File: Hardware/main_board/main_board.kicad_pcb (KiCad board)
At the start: 2 copper layers, 120 x 51.7 mm, 116 parts, among them J1 ALARM, J2 RFID_CONN, J3 GPS_CONN, J4 USB_A, J5 DEBUG, J6 ANTENNA2, J7 Conn_01x08_Male, J8 BATT, J9 RFShield_TwoPieces, Q1 2N3904, SW1 SW_Push, SW2 SW_Push, U1 STM32WL55_UFQFPN48, U2 FT201XQ, U3 SKY13370-374LF, U4 ID-3LA, U5 AP7370-50W5-7, U6 S-1135A33-M5T1U, U7 AP22811BW5-7, U8 AP22811BW5-7, U9 74LVC1G04, Y1 32MHz

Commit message: finished main board
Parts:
- removed ANTENNA1: 1.337m, Connector_Coaxial:SMA_Amphenol_132289_EdgeMount
- removed C11, C35: 10n, Capacitor_SMD:C_0805_2012Metric
- removed C12, C13: 47p, Capacitor_SMD:C_0805_2012Metric
- removed C14: 0.1u, Capacitor_SMD:C_0805_2012Metric
- removed C15, C18: 100n, Capacitor_SMD:C_0805_2012Metric
- removed C16: 4.7u, Capacitor_SMD:C_0805_2012Metric
- removed C36, C46: 1u, Capacitor_SMD:C_0805_2012Metric
- removed C37: DNP, Capacitor_SMD:C_0805_2012Metric
- removed D2, D3: LED, LED_SMD:LED_0805_2012Metric
- removed FB1: FerriteBead, LED_SMD:LED_0805_2012Metric
- removed J4: USB_A, Connector_USB:USB_A_Molex_67643_Horizontal
- removed J9: RFShield_TwoPieces, Capacitor_SMD:C_0805_2012Metric
- removed JP5: SolderJumper_2_Open, Jumper:SolderJumper-2_P1.3mm_Open_TrianglePad1.0x1.5mm
- removed JP8: SolderJumper_3_Open, Jumper:SolderJumper-3_P2.0mm_Open_TrianglePad1.0x1.5mm
- removed Q1: 2N3904, Package_TO_SOT_THT:TO-92_Inline
- removed R10, R11, R5, R6: 1k, Resistor_SMD:R_0805_2012Metric_Pad1.20x1.40mm_HandSolder
- removed R2, R3: 27R, Resistor_SMD:R_0805_2012Metric_Pad1.20x1.40mm_HandSolder
- removed R4: 5k, Resistor_SMD:R_0805_2012Metric_Pad1.20x1.40mm_HandSolder
- removed R7: 500R, Resistor_SMD:R_0805_2012Metric_Pad1.20x1.40mm_HandSolder
- removed R8: 15R, Resistor_SMD:R_0805_2012Metric_Pad1.20x1.40mm_HandSolder
- removed R9: 300R, Resistor_SMD:R_0805_2012Metric_Pad1.20x1.40mm_HandSolder
- removed SW2: SW_Push, Connector_PinSocket_2.54mm:PinSocket_1x02_P2.54mm_Vertical
- removed TP11, TP12: TestPoint, Connector_PinHeader_2.54mm:PinHeader_1x01_P2.54mm_Vertical
- removed U2: FT201XQ, Package_DFN_QFN:QFN-16-1EP_4x4mm_P0.65mm_EP2.1x2.1mm
- removed U4: ID-3LA, new_footprints:ID-3LA
- removed U9: 74LVC1G04, Package_TO_SOT_SMD:SOT-23-5_HandSoldering
- added H1: MountingHole_Pad, MountingHole:MountingHole_2.2mm_M2_DIN965_Pad, F.Cu at (137.7, 147.2)
- added H2: MountingHole_Pad, MountingHole:MountingHole_2.2mm_M2_DIN965_Pad, F.Cu at (221.4, 134.9)
- added H4: MountingHole_Pad, MountingHole:MountingHole_2.2mm_M2_DIN965_Pad, F.Cu at (221.4, 146.3)
- added TP20: TestPoint, TestPoint:TestPoint_Pad_1.0x1.0mm, F.Cu at (174.3, 147.9)
- added TP21: TestPoint, TestPoint:TestPoint_Pad_1.0x1.0mm, F.Cu at (166.4, 147.5)
- added TP8: TestPoint, TestPoint:TestPoint_Pad_1.0x1.0mm, F.Cu at (169.0, 142.2)
- added TP9: TestPoint, TestPoint:TestPoint_Pad_1.0x1.0mm, F.Cu at (174.7, 135.9)
- C10, C17, C22, C23, C24, C25, C26, C27, C28, C29, C3, C30, C31, C32, C33, C34, C38, C39, C4, C40, C41, C42, C43, C5, C6, C7, C8, C9: footprint Capacitor_SMD:C_0805_2012Metric -> Capacitor_SMD:C_0603_1608Metric
- J7: value Conn_01x08_Male -> Conn_01x04_Male; footprint Connector_PinHeader_2.54mm:PinHeader_2x04_P2.54mm_Vertical -> Connector_PinHeader_1.27mm:PinHeader_1x04_P1.27mm_Vertical
- JP1, JP2, JP3, JP4: footprint Jumper:SolderJumper-2_P1.3mm_Open_TrianglePad1.0x1.5mm -> new_footprints:tinyjumper
- TP1, TP13, TP14, TP2, TP3, TP4, TP5, TP6, TP7: footprint Connector_PinHeader_2.54mm:PinHeader_1x01_P2.54mm_Vertical -> TestPoint:TestPoint_Pad_1.0x1.0mm
- moved J7 116.0 mm to (162.6, 148.7), turned to -90 degrees
- moved TP4 35.7 mm to (163.3, 140.6)
- moved TP13 34.0 mm to (142.9, 146.2)
- moved TP2 33.6 mm to (165.6, 142.0)
- moved TP3 33.4 mm to (171.1, 142.2)
- moved SW1 31.4 mm to (132.9, 145.7), turned to 180 degrees
- moved TP7 22.3 mm to (160.9, 140.6)
- moved TP6 19.4 mm to (163.3, 145.1)
- moved J8 17.6 mm to (132.1, 138.9), turned to 180 degrees
- moved J5 16.2 mm to (136.1, 139.1)
- moved TP14 15.1 mm to (133.4, 133.3)
- moved C45 13.7 mm to (149.1, 134.5), turned to 180 degrees
- moved TP5 13.5 mm to (161.1, 145.1)
- moved C44 9.75 mm to (146.3, 148.1), turned to 180 degrees
- moved D4 9.28 mm to (129.2, 144.3), turned to 90 degrees
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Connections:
- J7 pad 1: +3V3_RFID -> I2C1_SCL
- J7 pad 2: Net-(J7-Pad2) -> I2C1_SDA
- J7 pad 3: Net-(J7-Pad3) -> +3V3
- J7 pad 4: Net-(J7-Pad4) -> GND
- TP3 pad 1: Net-(TP3-Pad1) -> DEBUG_JTDI
- U1 pad 12: Net-(TP3-Pad1) -> unconnected-(U1-Pad12)
- U1 pad 31: unconnected-(U1-Pad31) -> RFSW_VC2
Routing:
- net RFSW_VC1: track 7.34 -> 73.1 mm, vias 0 -> 2
- net NRST: track 9.89 -> 72.5 mm, vias 0 -> 1
- net RFID_~{PWR}: track 2.39 -> 50.1 mm, vias 1 -> 2
- net +3V3: track 131.7 -> 177.5 mm, vias 7 -> 4
- net ALARM_ON: track 0.00 -> 45.1 mm, vias 0 -> 1
- net RFSW_VC2: track 12.6 -> 57.4 mm, vias 0 -> 2
- net +5V: track 1.85 -> 43.9 mm, vias 0 -> 3
- net GPS_~{PWR}: track 0.95 -> 41.9 mm, vias 1 -> 2
- net RFID_DATA1: track 0.00 -> 35.4 mm, vias 0 -> 1
- net RFID_DATA0: track 0.00 -> 30.6 mm, vias 0 -> 1
- net RFID_TAG_IN_RANGE: track 0.00 -> 28.7 mm, vias 0 -> 1
- net Net-(TP6-Pad1): track 2.49 -> 29.1 mm, vias 1 -> 2
- net Net-(TP2-Pad1): track 4.34 -> 30.9 mm, vias 1 -> 2
- net RFID_NRST: track 0.00 -> 24.9 mm, vias 0 -> 1
- net DEBUG_JTCK_SWCLK: track 23.5 -> 47.4 mm
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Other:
- board size 120 x 51.7 mm -> 107.1 x 18.1 mm
- board text added: "ALARM"
- board text added: "BATT"
- board text added: "Concealed Bike Anti-Theft Device"
- board text added: "DEBUG"
- board text added: "EATKINSO"
- board text added: "ECE 445 SP22"
- board text added: "GPS"
- board text added: "Group 45"
- board text added: "RFID"
- board text added: "RFID ON"
- board text added: "v0.0.1"

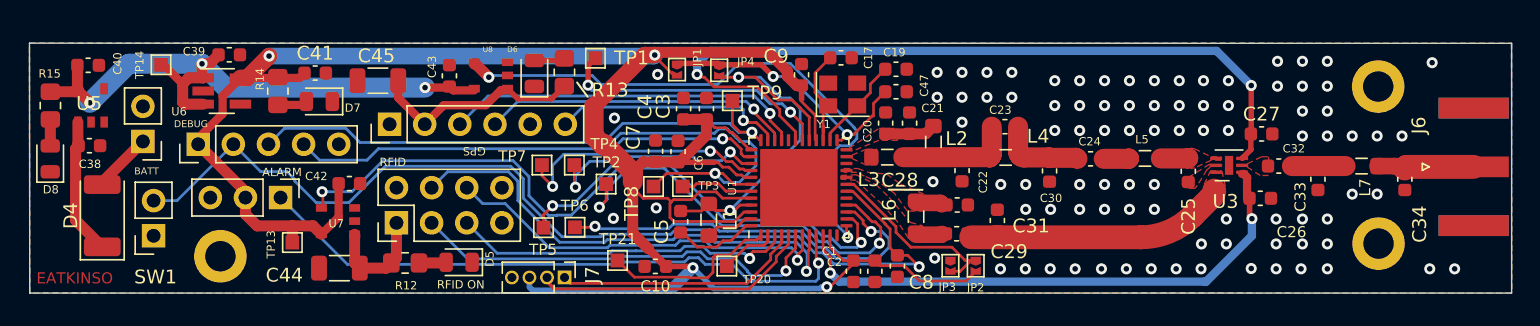
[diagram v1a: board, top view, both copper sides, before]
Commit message: all boards pass DRC and have appropriate silkscreens, will order tomorrow
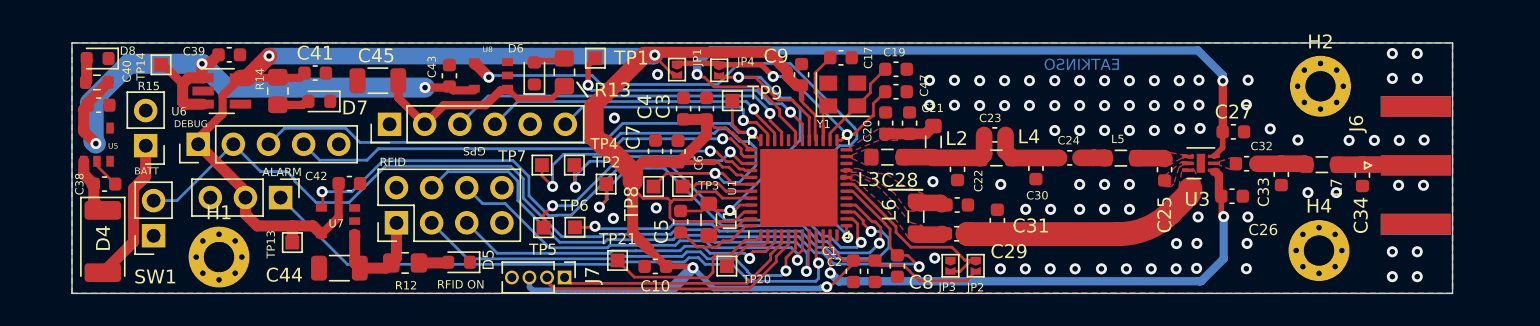
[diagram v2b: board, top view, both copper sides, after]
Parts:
- D5, D6, D7, D8: footprint LED_SMD:LED_0805_2012Metric -> LED_SMD:LED_0603_1608Metric
- H1, H2, H4: footprint MountingHole:MountingHole_2.2mm_M2_DIN965_Pad -> MountingHole:MountingHole_2.2mm_M2_Pad_Via
- R15: footprint Resistor_SMD:R_0805_2012Metric_Pad1.20x1.40mm_HandSolder -> Resistor_SMD:R_0603_1608Metric
- moved D8 8.02 mm to (128.8, 132.9), turned to 180 degrees
- moved H4 4.33 mm to (217.1, 146.8)
- moved J6 4.18 mm to (224.1, 140.6)
- moved H2 4.17 mm to (217.2, 134.9)
- moved R15 3.76 mm to (128.8, 134.6), turned to 0 degrees
- moved C34 3.08 mm to (220.2, 141.3)
- moved C40 2.98 mm to (128.9, 136.3)
- moved C38 2.98 mm to (129.3, 142.0)
- moved L7 2.87 mm to (217.3, 140.6)
- moved U5 2.87 mm to (127.7, 140.3)
- moved C33 2.67 mm to (214.4, 141.3)
- moved C32 2.33 mm to (211.9, 140.5)
- moved C26 2.05 mm to (210.8, 142.9)
- moved C27 2.05 mm to (210.9, 138.2)
- moved U3 2.05 mm to (208.6, 140.5)
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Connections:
- U5 pad 3: GND -> unconnected-(U5-Pad3)
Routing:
- net RFSW_VC1: track 73.1 -> 40.2 mm
- net Net-(D4-Pad2): track 4.16 -> 11.4 mm
- net Net-(C38-Pad1): track 9.93 -> 4.91 mm
- net +5V: track 43.9 -> 47.2 mm
- net GND: track 6.05 -> 8.25 mm, vias 91 -> 80
- net RFSW_VC2: track 57.4 -> 55.6 mm
- net Net-(C29-Pad2): track 18.8 -> 17.5 mm
- net Net-(C34-Pad1): track 7.00 -> 5.80 mm
- net Net-(C22-Pad1): track 8.52 -> 7.38 mm
- net Net-(C23-Pad2): track 6.36 -> 5.25 mm
- net (no net): vias 0 -> 1
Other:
- board size 107.1 x 18.1 mm -> 99.8 x 18.1 mm
